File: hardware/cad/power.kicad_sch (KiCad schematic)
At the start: 37 parts, among them J21 2P_HEADER, J22 2P_HEADER, U7 TLV767, U8 LT3463, U9 LT3032

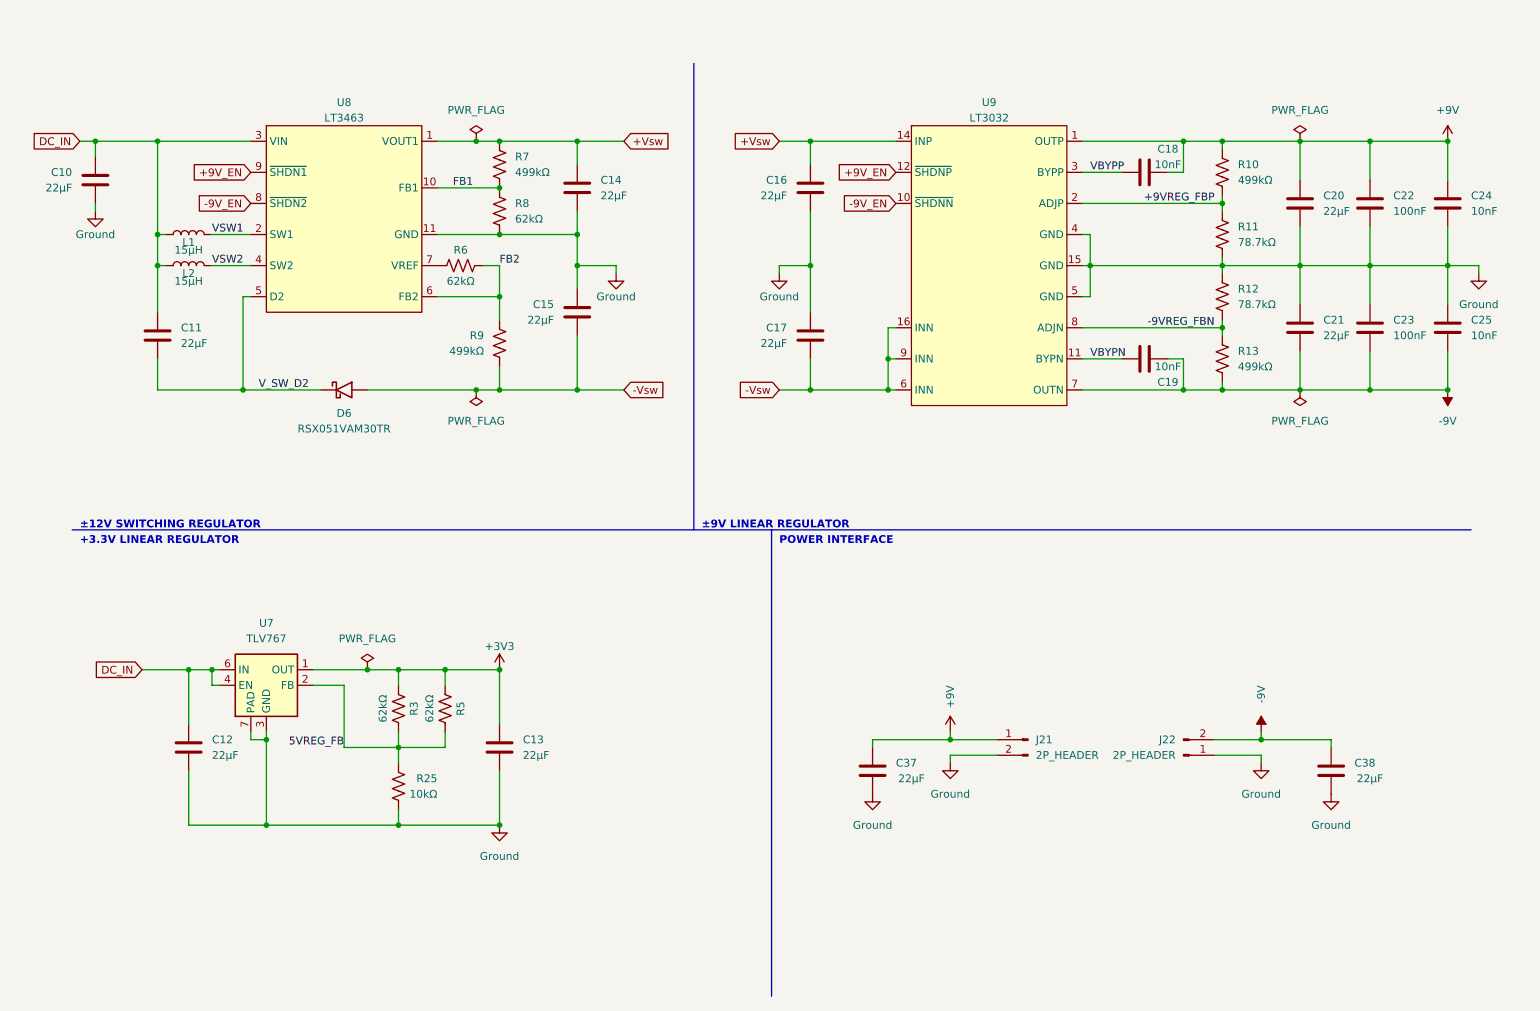
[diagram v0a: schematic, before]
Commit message: added differential inputs and started new layout
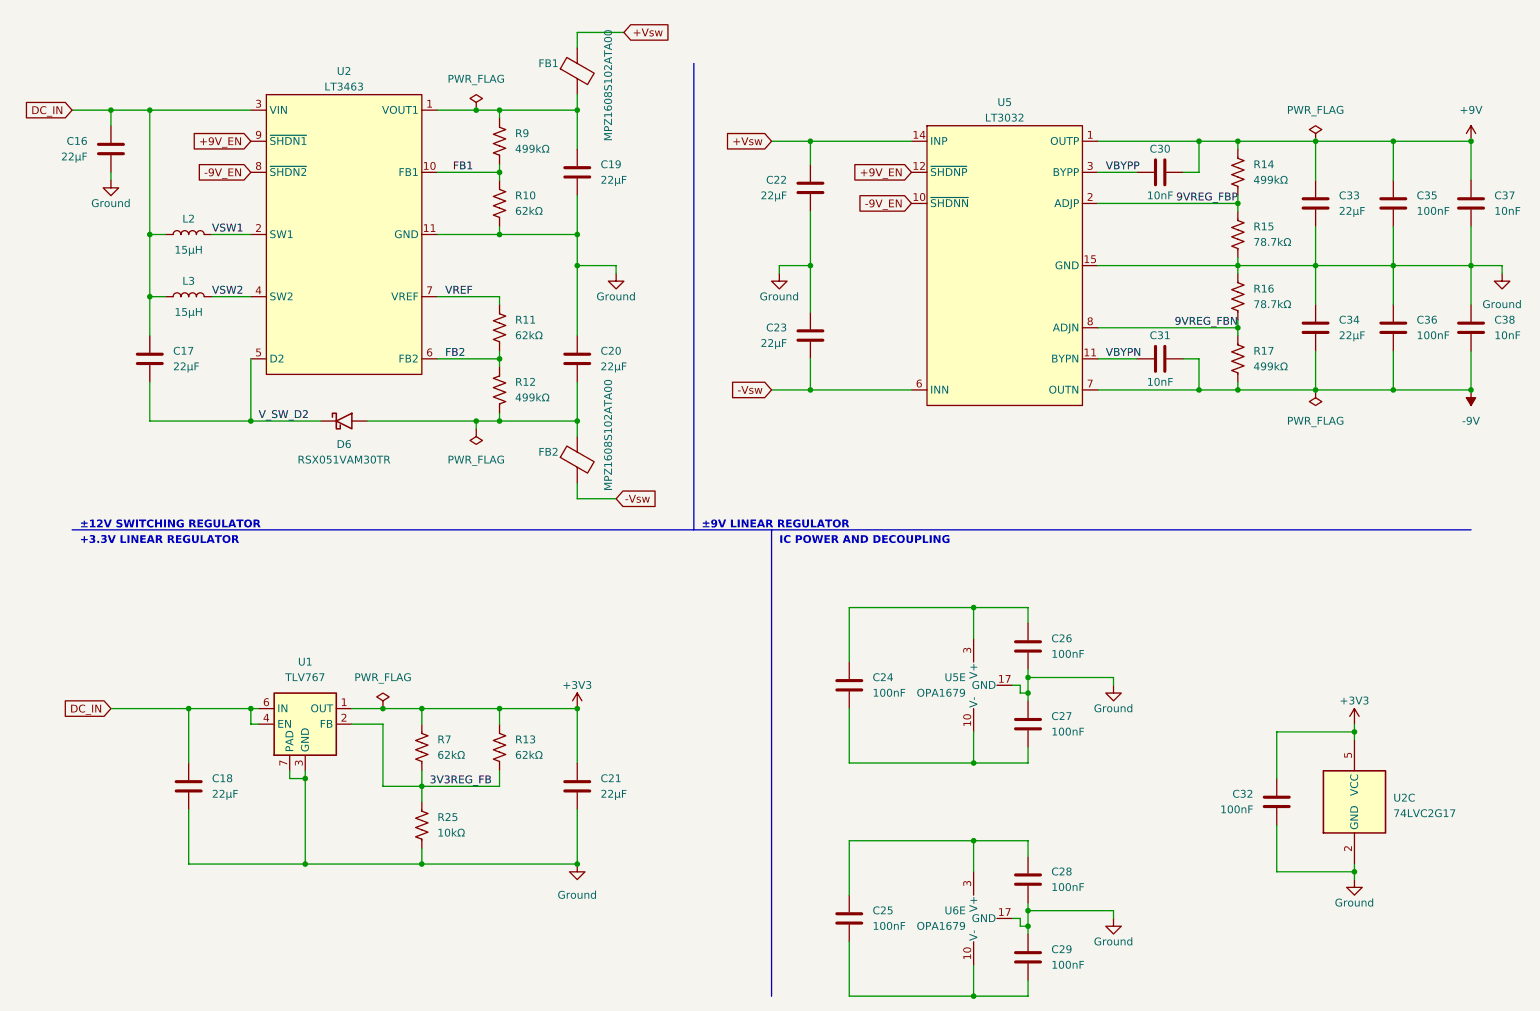
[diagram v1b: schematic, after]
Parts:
- removed C10, C11, C12, C13, C14, C15: 22μF, Capacitor_SMD:C_0805_2012Metric, symbol Device:C
- removed J21, J22: 2P_HEADER, Connector_PinSocket_2.54mm:PinSocket_1x02_P2.54mm_Vertical, symbol Connector:Conn_01x02_Male
- removed L1: 15μH, Library:L_Taiyo-Yuden_NR-24xx, symbol Device:L
- removed R3, R5, R6, R8: 62kΩ, Resistor_SMD:R_0603_1608Metric, symbol Device:R_US
- removed U7: TLV767, Library:WSON-6-1EP_2x2mm_P0.65mm_EP1x1.6mm_ThermalVias, symbol Regulator_Linear:TLV76701DRVx
- removed U8: LT3463, Library:DFN-10-1EP_3x3mm_P0.5mm_EP1.65x2.38mm_ThermalVias, symbol Library:LT3463
- removed U9: LT3032, Library:DE14MA, symbol Library:LT3032
- added C26, C27, C28, C29, C35, C36: 100nF, Capacitor_SMD:C_0805_2012Metric, symbol Device:C
- added C30, C31: 10nF, Capacitor_SMD:C_0603_1608Metric, symbol Device:C
- added C32: 100nF, Capacitor_SMD:C_0603_1608Metric, symbol Device:C
- added C33, C34: 22μF, Capacitor_SMD:C_0805_2012Metric, symbol Device:C
- added FB1, FB2: MPZ1608S102ATA00, Resistor_SMD:R_0603_1608Metric, symbol Device:FerriteBead
- added L3: 15μH, Library:L_Taiyo-Yuden_NR-24xx, symbol Device:L
- added R14, R17: 499kΩ, Resistor_SMD:R_0603_1608Metric, symbol Device:R_US
- added R15, R16: 78.7kΩ, Resistor_SMD:R_0603_1608Metric, symbol Device:R_US
- added U1: TLV767, Library:WSON-6-1EP_2x2mm_P0.65mm_EP1x1.6mm_ThermalVias, symbol Regulator_Linear:TLV76701DRVx
- added U2: LT3463, Package_DFN_QFN:DFN-10-1EP_3x3mm_P0.5mm_EP1.65x2.38mm_ThermalVias, symbol Library:LT3463
- added U5: LT3032, Library:DE14MA, symbol Library:LT3032
- added U6: OPA1679, Library:OPA1679, symbol Library:OPA1679
- C18, C19: value 10nF -> 22μF; footprint Capacitor_SMD:C_0603_1608Metric -> Capacitor_SMD:C_0805_2012Metric; Part Number GRM1885C1H103JA01J -> GRM21BR61E226ME44L
- C22, C23: value 100nF -> 22μF; Part Number GRM31C5C1H104JA01K -> GRM21BR61E226ME44L
- C24, C25: value 10nF -> 100nF; footprint Capacitor_SMD:C_0603_1608Metric -> Capacitor_SMD:C_0805_2012Metric; Part Number GRM1885C1H103JA01J -> GRM31C5C1H104JA01K
- C37, C38: value 22μF -> 10nF; footprint Capacitor_SMD:C_0805_2012Metric -> Capacitor_SMD:C_0603_1608Metric; Part Number GRM21BR61E226ME44L -> GRM1885C1H103JA01J
- R10, R13, R7: value 499kΩ -> 62kΩ; Part Number RN73H1JTTD4993F100 -> RN73H1JTTD6202F100
- R11: value 78.7kΩ -> 62kΩ; Part Number RN73H1JTTD7772F100 -> RN73H1JTTD6202F100
- R12: value 78.7kΩ -> 499kΩ; Part Number RN73H1JTTD7772F100 -> RN73H1JTTD4993F100
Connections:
- net +3V3: now also C21.2, R13.1, R7.1, C32.2, U1.1 (OUT), U2.5 (VCC)
- net +9V: now also C37.1, C30.1, C33.2, C35.2, R14.1, U5.1 (OUTP); no longer C18.1, C20.2, C22.2, C24.1, C37.2, R10.1
- net +9V_EN: now also U2.9 (~{SHDN1}), U5.12 (~{SHDNP})
- net +Vsw: now also C22.2, FB1.1, U5.14 (INP); no longer C16.2, R7.1
- net -9V: now also C31.1, C34.1, C36.1, R17.2, U5.7 (OUTN); no longer C19.1, C21.1, C23.1, C25.2, R13.2
- net -9V_EN: now also U2.8 (~{SHDN2}), U5.10 (~{SHDNN})
- net DC_IN: now also C16.2, C17.2, C18.2, L2.2, L3.1, U1.4 (EN), U1.6 (IN), U2.3 (VIN); no longer L2.1
- net FB1: now also R10.1, R9.2, U2.10 (FB1); no longer R7.2
- net FB2: now also R11.1, R12.1, U2.6 (FB2); no longer R9.1
- net GND: now also C18.1, C19.1, C20.2, C21.1, C37.2, R10.2, C26.1, C27.2, C28.1, C29.2, C32.1, C33.1, C34.2, C35.1, C36.2, R15.2, R16.1, U1.3 (GND), U1.5 (GND), U1.7 (PAD), U2.11 (GND), U2.2 (GND), U5.15 (GND), U5.17 (GND), U5.4 (GND), U5.5 (GND), U6.17 (GND); no longer C17.2, C20.1, C21.2, C24.2, C25.1, C37.1, R11.2, R12.1
- net VBYPN: now also C31.2, U5.11 (BYPN); no longer C19.2
- net VBYPP: now also C30.2, U5.3 (BYPP); no longer C18.2
- net VSW1: now also L2.1, U2.2 (SW1)
- net VSW2: now also L3.2, U2.4 (SW2); no longer L2.2
- net V_SW_D2: now also C17.1, U2.5 (D2)
- removed net +9VREG_FBP: R10.2, R11.1
- net -9VREG_FBN: no longer names the net of R12.2
- net -9VREG_FBN: now also C20.1, D6.2 (A), FB2.1; no longer R13.1
- removed net -Vsw: C17.1, D6.2 (A), R9.2
- net 5VREG_FB renamed 3V3REG_FB
- net 3V3REG_FB: now also R13.2, R7.2, U1.2 (FB)
- new net: C25.1, C29.1, U6.10 (V-)
- new net: C25.2, C28.2, U6.3 (V+)
- new net: C19.2, FB1.2, R9.1, U2.1 (VOUT1)
- new net: C24.2, C26.2, U5.3 (V+)
- new net: C24.1, C27.1, U5.10 (V-)
- new net 9VREG_FBN: R16.2, R17.1, U5.8 (ADJN)
- new net 9VREG_FBP: R14.2, R15.1, U5.2 (ADJP)
- new net INN: C23.1, FB2.2, U5.16 (INN), U5.6 (INN), U5.9 (INN)
- new net VREF: R11.2, U2.7 (VREF)
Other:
- note added: "IC POWER AND DECOUPLING"
- note removed: "POWER INTERFACE"

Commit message: more layout updates
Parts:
- removed C24, C25: 100nF, Capacitor_SMD:C_0805_2012Metric, symbol Device:C
- C16, C17, C18, C19, C20, C21, C22, C23: value 22μF -> 22u
- C24: renamed from C26; value 100nF -> 100n
- C25: renamed from C27; value 100nF -> 100n
- C26: renamed from C28; value 100nF -> 100n
- C27: renamed from C29; value 100nF -> 100n
- C28: renamed from C30; value 10nF -> 10n
- C29: renamed from C31; value 10nF -> 10n
- C30: renamed from C32; value 100nF -> 100n
- C31: renamed from C33; value 22μF -> 22u
- C32: renamed from C34; value 22μF -> 22u
- C33: renamed from C35; value 100nF -> 100n
- C34: renamed from C36; value 100nF -> 100n
- C35: renamed from C37; value 10nF -> 10n
- C36: renamed from C38; value 10nF -> 10n
- L2, L3: value 15μH -> 15u
- R10, R11, R13, R7: value 62kΩ -> 62k
- R12, R14, R17, R9: value 499kΩ -> 499k
- R15, R16: value 78.7kΩ -> 78.7k
- R25: value 10kΩ -> 10k
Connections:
- net +9V: now also C24.2, C26.2, U5.3 (V+), U6.3 (V+)
- net -9V: now also C25.1, C27.1, U5.10 (V-), U6.10 (V-)

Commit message: reorganized project
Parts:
- removed C16, C17, C18, C19, C20, C21, C22, C23, C31, C32: 22u, Capacitor_SMD:C_0805_2012Metric, symbol Device:C
- removed C24, C25, C26, C27, C33, C34: 100n, Capacitor_SMD:C_0805_2012Metric, symbol Device:C
- removed C28, C29, C35, C36: 10n, Capacitor_SMD:C_0603_1608Metric, symbol Device:C
- removed C30: 100n, Capacitor_SMD:C_0603_1608Metric, symbol Device:C
- removed D6: RSX051VAM30TR, Library:SOD-323HE, symbol Library:RSX051VAM30TR
- removed FB1, FB2: MPZ1608S102ATA00, Resistor_SMD:R_0603_1608Metric, symbol Device:FerriteBead
- removed L2, L3: 15u, Library:L_Taiyo-Yuden_NR-24xx, symbol Device:L
- removed R10, R11, R13, R7: 62k, Resistor_SMD:R_0603_1608Metric, symbol Device:R_US
- removed R12, R17, R9: 499k, Resistor_SMD:R_0603_1608Metric, symbol Device:R_US
- removed R16: 78.7k, Resistor_SMD:R_0603_1608Metric, symbol Device:R_US
- removed R25: 10k, Resistor_SMD:R_0603_1608Metric, symbol Device:R_US
- removed U1: TLV767, Library:WSON-6-1EP_2x2mm_P0.65mm_EP1x1.6mm_ThermalVias, symbol Regulator_Linear:TLV76701DRVx
- removed U2: LT3463, Package_DFN_QFN:DFN-10-1EP_3x3mm_P0.5mm_EP1.65x2.38mm_ThermalVias, symbol Library:LT3463
- removed U5: LT3032, Library:DE14MA, symbol Library:LT3032
- removed U6: OPA1679, Library:OPA1679, symbol Library:OPA1679
- added C201: 150p, Capacitor_SMD:C_0805_2012Metric, symbol Device:C
- added C401, C404, C405, C406, C408, C409, C413, C415, C416, C417, C418, C419: 22µ, Capacitor_SMD:C_1210_3225Metric, symbol Device:C
- added C403, C407, C412, C414: 2.2µ, Capacitor_SMD:C_0603_1608Metric, symbol Device:C
- added C410: 2n, Capacitor_SMD:C_0603_1608Metric, symbol Device:C
- added C411: 39n, Capacitor_SMD:C_0603_1608Metric, symbol Device:C
- added CHS201: Chassis, Library:Harwin_EMI_Finger_S7061-46R, symbol Library:Chassis
- added D203: DFLZ13Q-7, Library:D_PowerDI-123_THERMAL_PAD, symbol Library:DFLZ13Q-7
- added D402, D403: DFLS240L-7, Library:D_PowerDI-123_THERMAL_PAD, symbol Library:RSX051VAM30TR
- added J401: Jack-DC, Library:CUI_PJ-063AH, symbol Connector:Jack-DC
- added L401, L402: 22µ, Inductor_SMD:L_Bourns_SRP5030T, symbol Device:L
- added NT401: NetTie_2, Library:Net_Tie, symbol Device:NetTie_2
- added R401: 750R, Resistor_SMD:R_0402_1005Metric, symbol Device:R_US
- added R402, R410: 120R, Resistor_SMD:R_0402_1005Metric, symbol Device:R_US
- added R405: 18k, Resistor_SMD:R_0402_1005Metric, symbol Device:R_US
- added R406: 1.8k, Resistor_SMD:R_0402_1005Metric, symbol Device:R_US
- added R407, R412: 100k, Resistor_SMD:R_0402_1005Metric, symbol Device:R_US
- added R408: 200R, Resistor_SMD:R_0603_1608Metric, symbol Device:R_US
- added R409: 71.5k, Resistor_SMD:R_0402_1005Metric, symbol Device:R_US
- added R411: 1.4M, Resistor_SMD:R_0402_1005Metric, symbol Device:R_US
- added R413: 1.15M, Resistor_SMD:R_0402_1005Metric, symbol Device:R_US
- added TP203, TP204, TP403, TP404, TP405: TestPoint, TestPoint:TestPoint_Pad_D1.0mm, symbol Connector:TestPoint
- added U401: LM337, Package_TO_SOT_SMD:SOT-223-3_TabPin2, symbol Regulator_Linear:LM337_TO252
- added U402, U404: LM317, Package_TO_SOT_SMD:SOT-223-3_TabPin2, symbol Regulator_Linear:LM317_TO-252
- added U403: ADP5070, Library:LFCSP-20-1EP_4x4mm_P0.5mm_EP2.6x2.6mm, symbol Library:ADP5070ACPZ
- R403: renamed from R15; value 78.7k -> 750R; footprint Resistor_SMD:R_0603_1608Metric -> Resistor_SMD:R_0402_1005Metric; Manufacturer Koa Speer -> KOA Speer Electronics; Part Number RN73H1JTTD7772F100 -> (none)
- R404: renamed from R14; value 499k -> 120R; footprint Resistor_SMD:R_0603_1608Metric -> Resistor_SMD:R_0402_1005Metric; Manufacturer Koa Speer -> KOA Speer Electronics; Part Number RN73H1JTTD4993F100 -> (none)
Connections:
- net +3V3: now also C415.2, R410.1, TP405.1, U404.2 (VO)
- net +9V: now also C409.2, TP404.1, U402.2 (VO)
- net +9V_EN: now also U403.7 (EN1)
- net -9V: now also C404.2, R402.1, TP403.1, U401.3 (VO)
- net -9V_EN: now also U403.9 (EN2)
- net 3V3REG_FB: now also C414.2, R408.1, R410.2, U404.1 (ADJ)
- net DC_IN: now also C201.1, C405.1, C408.2, C413.2, D203.1 (K), J401.2, TP204.1, U403.15 (PVIN1), U403.16 (PVINSYS), U403.17 (PVIN2), U404.3 (VI)
- net GND: now also C201.2, C403.1, C404.1, C405.2, C407.1, C409.1, C410.1, C411.1, C412.1, C413.1, C414.1, C415.1, CHS201., D203.2 (A), J401.1, NT401.1, R401.2, R407.1, R408.2, R412.1, TP203.1, U403.13 (AGND), U403.2 (SYNC/FREQ), U403.21 (AGND), U403.4 (SLEW)
- net VSW1: now also L401.2, U403.1 (INBK)
- net VSW2: now also D403.1 (K), L402.2, U403.18 (SW2)
- net 9VREG_FBP renamed +9VREG_FBP
- net +9VREG_FBP: now also C407.2, U402.1 (ADJ)
- new net: C410.2, R405.1
- new net: D402.2 (A), L401.1, U403.20 (SW1)
- new net: C411.2, R406.1
- new net +12V_RAW: C406.2, C416.2, C418.2, D402.1 (K), R411.2, U402.3 (VI)
- new net -12V_RAW: C401.2, C417.2, C419.2, D403.2 (A), R413.1, U401.2 (VI)
- new net -9VREG_FBN: C403.2, R401.1, R402.2, U401.1 (ADJ)
- new net GND1: C401.1, C406.1, C408.1, C416.1, C417.1, C418.1, C419.1, L402.1, NT401.2, U403.19 (PGND)
- new net VSW_COMP1: R405.2, U403.6 (COMP1)
- new net VSW_COMP2: R406.2, U403.10 (COMP2)
- new net VSW_FB1: R411.1, R412.2, U403.5 (FB1)
- new net VSW_FB2: R409.1, R413.2, U403.11 (FB2)
- new net VSW_SOFT_START: R407.2, U403.8 (SS)
- new net VSW_VREF: R409.2, U403.12 (VREF)
- new net VSW_VREG: C412.2, U403.14 (VREG)
- no-connect marks 0 -> 1
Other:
- note added: "+3.3V Linear Regulator"
- note added: "+9V Linear Regulator"
- note added: "-9V Linear Regulator"
- note added: "9-12VDC CENTER NEGATIVE"
- note added: "MINIMIZE COPPER AREA FOR VSW1 AND VSW2 TRACES PLACE CAPACITORS AS CLOSE TO IC AS POSSIBLE PLACE INDUCTORS AWAY FROM OTHER COMPONENTS ROUTE ALL FEEDBACK TRACES FROM AS CLOSE TO OUTPUT CAPACITORS AS POSSIBLE ROUTE SWITCHER OUTPUT RETURN PATH AS SEPARATE GROUND POUR"
- note added: "Power Input"
- note added: "Soft Start Resistor R407 = 100k Soft Start Time = 25ms"
- note added: "±12V Switching Regulator"
- note removed: "+3.3V LINEAR REGULATOR"
- note removed: "IC POWER AND DECOUPLING"
- note removed: "±12V SWITCHING REGULATOR"
- note removed: "±9V LINEAR REGULATOR"
- moved on the sheet: R403, R404

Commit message: finalized schematic
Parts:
- removed C404, C405, C406, C408, C409, C413, C415, C416, C417, C418, C419: 22µ, Capacitor_SMD:C_1210_3225Metric, symbol Device:C
- removed C414: 2.2µ, Capacitor_SMD:C_0603_1608Metric, symbol Device:C
- removed R407, R412: 100k, Resistor_SMD:R_0402_1005Metric, symbol Device:R_US
- added C304, C305, C306, C307, C311, C313, C314, C315, C317, C318, C319, C320: 10µF, Capacitor_SMD:C_1210_3225Metric, symbol Device:C
- added C316: 2.2µF, Capacitor_SMD:C_0603_1608Metric, symbol Device:C
- added FID302: FIDUCIAL, Fiducial:Fiducial_0.5mm_Mask1mm, symbol Mechanical:Fiducial
- added L303: 22µH, Inductor_SMD:L_Bourns_SRP5030T, symbol Device:L
- added R307, R313: 71.5kΩ, Resistor_SMD:R_0402_1005Metric, symbol Device:R_US
- C201: value 150p -> 150pF
- C301: renamed from C401; value 22µ -> 10µF; Part Number GCM32EC71E226KE35 -> GRM32EC72A106KE05
- C303: renamed from C403; value 2.2µ -> 2.2µF
- C308: renamed from C410; value 2n -> 58nF
- C309: renamed from C407; value 2.2µ -> 2.2µF
- C310: renamed from C411; value 39n -> 10nF
- C312: renamed from C412; value 2.2µ -> 2.2µF
- CHS201: value Chassis -> CHASSIS
- J301: renamed from J401; value Jack-DC -> JACK, DC
- L301: renamed from L401; value 22µ -> 22µH
- L302: renamed from L402; value 22µ -> 22µH
- NT301: renamed from NT401; value NetTie_2 -> NET TIE
- R301: renamed from R401; value 750R -> 750Ω
- R302: renamed from R402; value 120R -> 120Ω
- R303: renamed from R403; value 750R -> 750Ω
- R304: renamed from R405; value 18k -> 33kΩ
- R305: renamed from R404; value 120R -> 120Ω
- R306: renamed from R406; value 1.8k -> 3.3kΩ
- R308: renamed from R408; value 200R -> 200Ω
- R309: renamed from R409; value 71.5k -> 62.5kΩ
- R310: renamed from R413; value 1.15M -> 1MΩ
- R311: renamed from R410; value 120R -> 120Ω
- R312: renamed from R411; value 1.4M -> 1MΩ
- TP203, TP204: value TestPoint -> TEST POINT; footprint TestPoint:TestPoint_Pad_D1.0mm -> TestPoint:TestPoint_Plated_Hole_D2.0mm
- TP303: renamed from TP403; value TestPoint -> TEST POINT; footprint TestPoint:TestPoint_Pad_D1.0mm -> TestPoint:TestPoint_Plated_Hole_D2.0mm
- TP304: renamed from TP404; value TestPoint -> TEST POINT; footprint TestPoint:TestPoint_Pad_D1.0mm -> TestPoint:TestPoint_Plated_Hole_D2.0mm
- TP305: renamed from TP405; value TestPoint -> TEST POINT; footprint TestPoint:TestPoint_Pad_D1.0mm -> TestPoint:TestPoint_Plated_Hole_D2.0mm
- renumbered D403 to D302, D402 to D303, U401 to U301, U402 to U302, U403 to U303, U404 to U304
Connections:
- net +12V_RAW: now also C306.2, C319.2, C320.2
- net +3V3: now also C318.2
- net +9V: now also C311.2
- net -12V_RAW: now also C315.2, C317.2
- net -9V: now also C304.2
- net 3V3REG_FB: now also C316.2
- net DC_IN: now also U303.2 (SYNC/FREQ), C305.2, C307.2, C313.2
- net GND: now also C301.1, C304.1, C305.1, C306.1, C311.1, C313.1, C316.1, C318.1, L303.1, R307.1, R313.1; no longer U303.2 (SYNC/FREQ)
- net GND1: now also C307.1, C315.1, C317.1, C319.1, C320.1; no longer C301.1
- net VSW1: now also L301.1; no longer L301.2
- net VSW_FB1: now also R313.2
- net VSW_SOFT_START: now also R307.2
- new net: C314.2, L301.2, U303.20 (SW1)
- new net: C314.1, D303.2 (A), L303.2
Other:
- note added: "+3.3V LINEAR REGULATOR"
- note added: "+9-12VDC CENTER NEGATIVE"
- note added: "+9V LINEAR REGULATOR"
- note added: "-9V LINEAR REGULATOR"
- note added: "MINIMIZE COPPER AREA FOR VSW1 AND VSW2 TRACES PLACE CAPACITORS AS CLOSE TO IC AS POSSIBLE PLACE INDUCTORS AWAY FROM OTHER COMPONENTS ROUTE ALL FEEDBACK TRACES FROM AS CLOSE TO OUTPUT CAPACITORS AS POSSIBLE MINIMIZE SWITCHER OUTPUT RETURN PATH COPPER AREA AND ROUTE AS SEPARATE GROUND POUR PLACE POWER AND ANALOG COMPONENTS NEAR EACH OTHER AND AWAY FROM OTHER CIRCUITS"
- note added: "POWER INPUT"
- note added: "SOFT START RESISTOR R407 = 71.5kΩ t_SS = 29ms"
- note added: "±12V 200mA SWITCHING REGULATOR"
- note removed: "+3.3V Linear Regulator"
- note removed: "+9V Linear Regulator"
- note removed: "-9V Linear Regulator"
- note removed: "9-12VDC CENTER NEGATIVE"
- note removed: "MINIMIZE COPPER AREA FOR VSW1 AND VSW2 TRACES PLACE CAPACITORS AS CLOSE TO IC AS POSSIBLE PLACE INDUCTORS AWAY FROM OTHER COMPONENTS ROUTE ALL FEEDBACK TRACES FROM AS CLOSE TO OUTPUT CAPACITORS AS POSSIBLE ROUTE SWITCHER OUTPUT RETURN PATH AS SEPARATE GROUND POUR"
- note removed: "Power Input"
- note removed: "Soft Start Resistor R407 = 100k Soft Start Time = 25ms"
- note removed: "±12V Switching Regulator"
- company: Alessandro Rizzoni -> ALESSANDRO RIZZONI
- title: Baseboard -> BASEBOARD
- moved on the sheet: C308, C310, C312, D302, L301, L302, NT301, R304, R306, R309, R310, U303
